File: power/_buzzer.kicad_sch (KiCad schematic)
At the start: 4 parts, among them Q1 SS8050

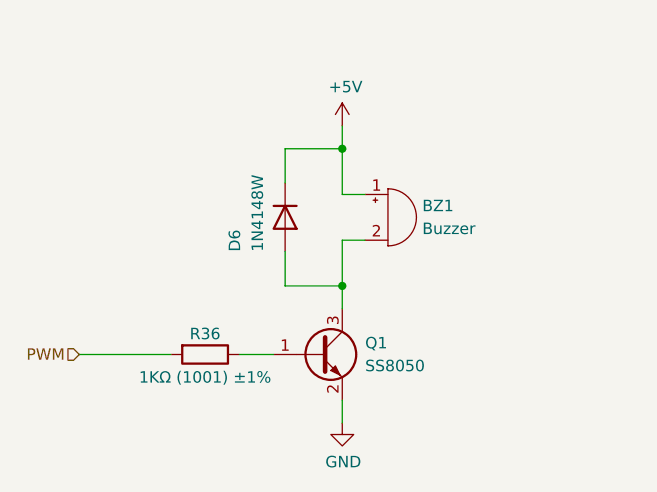
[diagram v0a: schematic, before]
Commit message: move buzzer to power board
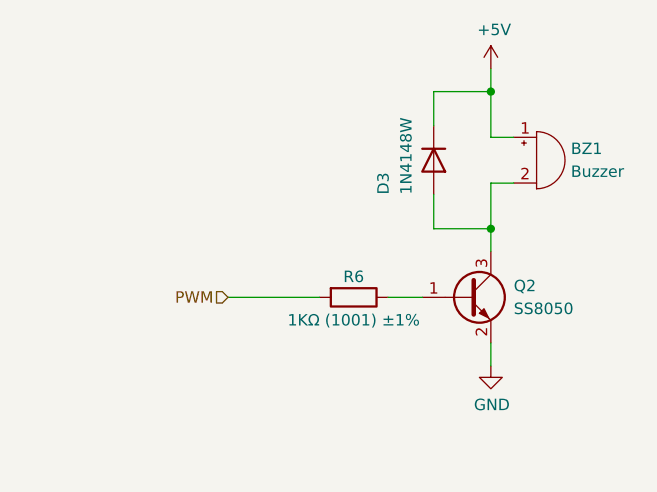
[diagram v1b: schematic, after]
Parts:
- removed D6: 1N4148W, Diode_SMD:D_SOD-123, symbol Diode:1N4148W
- removed Q1: SS8050, Package_TO_SOT_SMD:SOT-23, symbol Transistor_BJT:SS8050
- removed R36: 1KΩ (1001) ±1%, Resistor_SMD:R_0402_1005Metric, symbol Device:R
- added D3: 1N4148W, Diode_SMD:D_SOD-123, symbol Diode:1N4148W
- added Q2: SS8050, Package_TO_SOT_SMD:SOT-23, symbol Transistor_BJT:SS8050
- added R6: 1KΩ (1001) ±1%, Resistor_SMD:R_0402_1005Metric, symbol Device:R
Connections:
- net +5V: now also D3.1 (K)
- net GND: now also Q2.2 (E)
- net PWM: now also R6.2
- net at BZ1.2 (-): now also D3.2 (A), Q2.3 (C)
- new net: Q2.1 (B), R6.1
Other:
- title: (none) -> PilotPi: Power

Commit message: lots of changes
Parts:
- D3: Part (none) -> 1N4148W(KTP)
- Q2: value SS8050 -> BC847C; Part (none) -> BC847C,215
- R6: Part (none) -> SCR0402F1K
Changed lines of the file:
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@@
 		(date "15 nov 2012")
 		(rev "4")
+		(comment 1 "active buzzer with PWM input")
 	)
 	(junction
@@
 			)
 		)
-		(property "Part" ""
+		(property "Part" "SCR0402F1K"
 			(at 138.43 100.33 0)
 			(hide yes)
@@
 			)
 		)
+		(property "Part" "1N4148W(KTP)"
+			(at 147.32 85.09 0)
+			(hide yes)
+			(show_name no)
+			(do_not_autoplace no)
+			(effects
+				(font
+					(size 1.27 1.27)
+				)
+			)
+		)
 		(pin "1"
 		)
@@
 			)
 		)
-		(property "Value" "SS8050"
+		(property "Value" "BC847C"
 			(at 156.21 101.5999 0)
 			(show_name no)
@@
 			(at 151.13 100.33 0)
 			(hide yes)
+			(show_name no)
+			(do_not_autoplace no)
+			(effects
+				(font
+					(size 1.27 1.27)
+				)
+			)
+		)
+		(property "Part" "BC847C,215"
+			(at 151.13 100.33 0)
+			(hide yes)

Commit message: lots of changes
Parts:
- D3: Part 1N4148W(KTP) -> 1N4148W
- Q2: Part BC847C,215 -> SS8050(RANGE:200-350)
- R6: Part SCR0402F1K -> 0402WGF1001TCE
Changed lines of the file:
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@@
 			)
 		)
-		(property "Part" "SCR0402F1K"
+		(property "Part" "0402WGF1001TCE"
 			(at 138.43 100.33 0)
+			(hide yes)
+			(show_name no)
+			(do_not_autoplace no)
+			(effects
+				(font
+					(size 1.27 1.27)
+				)
+			)
+		)
+		(property "Field6" ""
+			(at 138.43 100.33 90)
 			(hide yes)
 			(show_name no)
@@
 			)
 		)
-		(property "Part" "1N4148W(KTP)"
+		(property "Part" "1N4148W"
 			(at 147.32 85.09 0)
 			(hide yes)
@@
 			)
 		)
-		(property "Part" "BC847C,215"
+		(property "Part" "SS8050(RANGE:200-350)"
 			(at 151.13 100.33 0)
 			(hide yes)
